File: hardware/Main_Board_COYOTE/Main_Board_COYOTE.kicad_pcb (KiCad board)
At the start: 2 copper layers, 198 x 138 mm, 57 parts, among them J1 Conn_01x05_Pin, J1 FTDI, J2 Conn_01x05_Pin, J3 Conn_01x05_Pin, J4 V+-, Q1 2N7002, SW1 SW_SPST, SW2 START, SW3 START, U1 QRE1113GR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

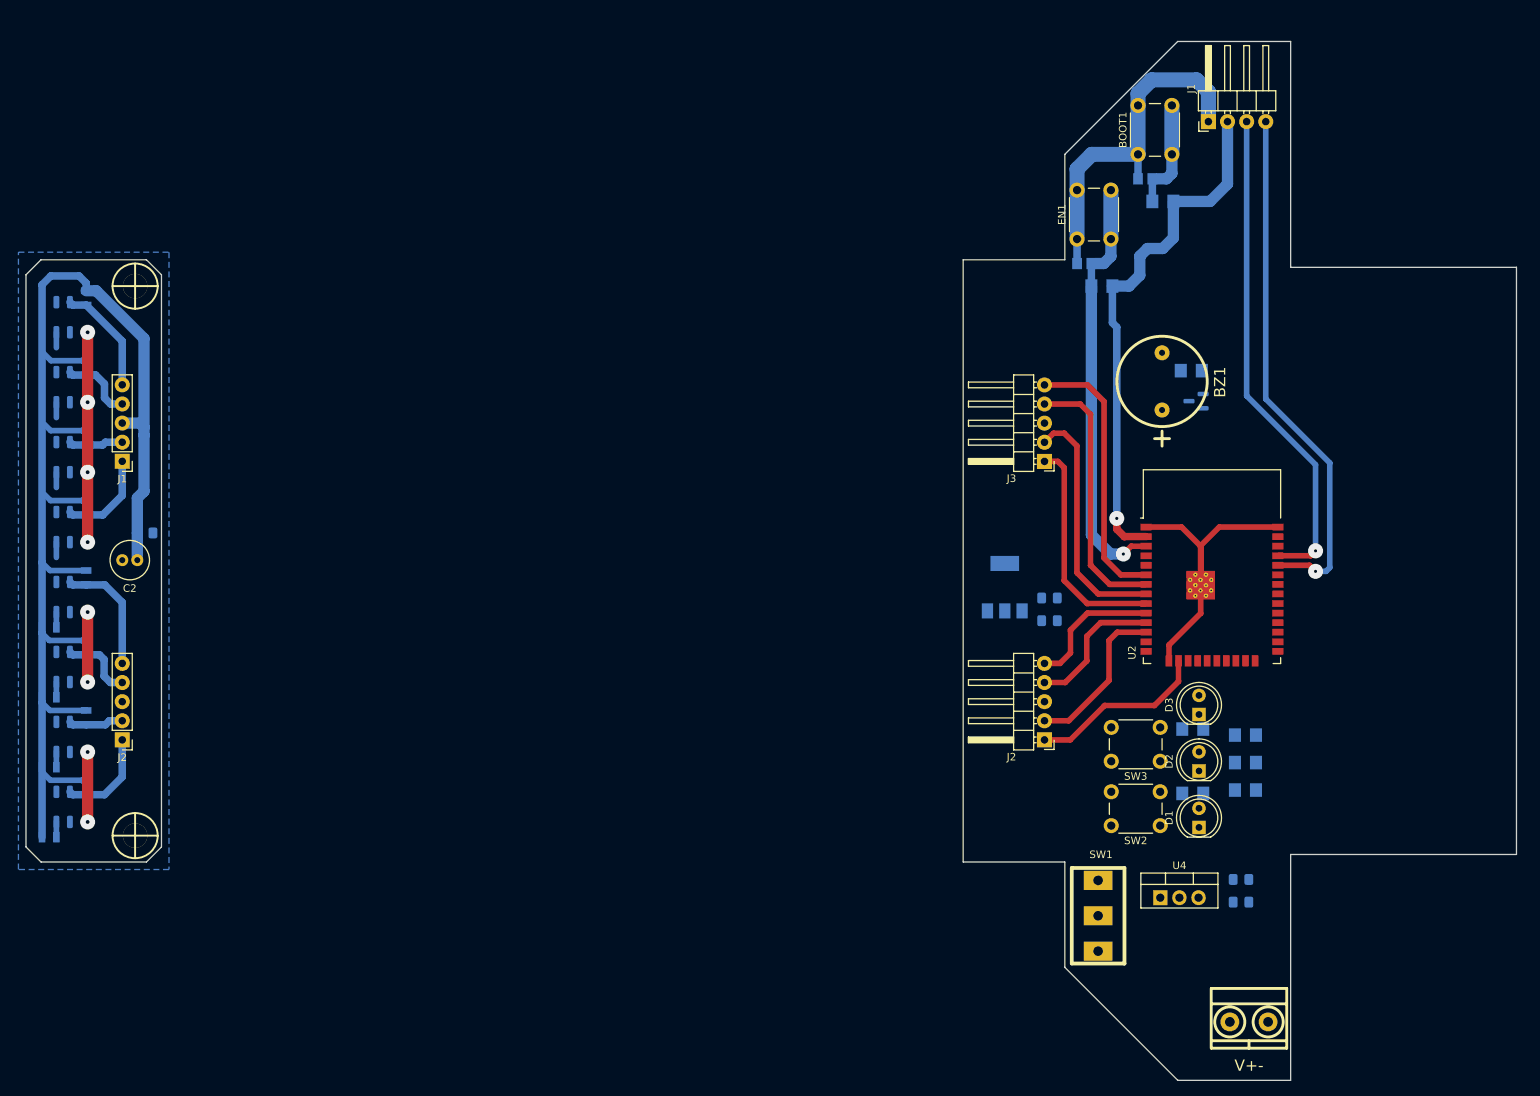
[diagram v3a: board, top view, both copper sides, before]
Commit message: SCH del velocista terminado
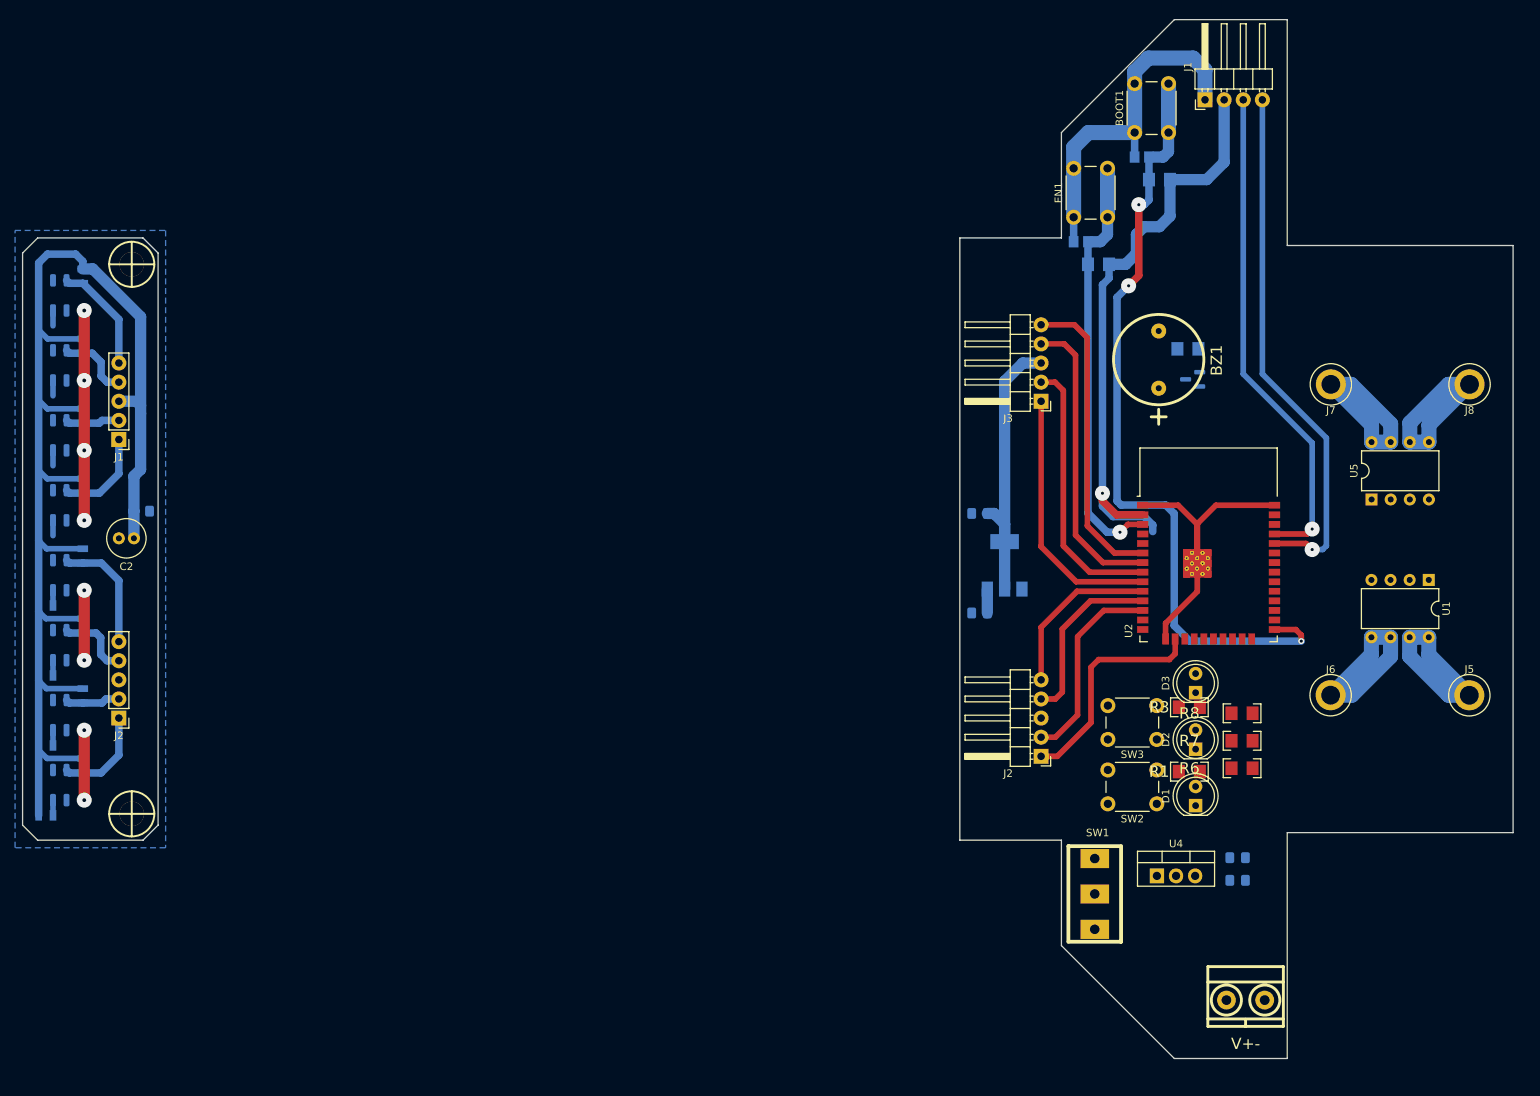
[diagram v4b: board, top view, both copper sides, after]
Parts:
- added J5: MOTOR_PINM1A, Connector:Banana_Jack_1Pin, F.Cu at (243.6, 110.8)
- added J6: MOTOR_PINM1B, Connector:Banana_Jack_1Pin, F.Cu at (225.2, 110.8)
- added J7: MOTOR_PINM1A, Connector:Banana_Jack_1Pin, F.Cu at (225.2, 69.5)
- added J8: MOTOR_PINM1B, Connector:Banana_Jack_1Pin, F.Cu at (243.6, 69.5)
- added U1: TA6586, Package_DIP:DIP-8_W7.62mm, F.Cu at (238.2, 95.5)
- added U5: TA6586, Package_DIP:DIP-8_W7.62mm, F.Cu at (230.6, 84.8)
- R1, R3, R6, R7, R8: moved to F.Cu
- moved C2 17.0 mm to (178.5, 86.7)
- moved C1 9.51 mm to (178.5, 99.9)
- moved J3 8.00 mm to (186.7, 71.8)
- moved R6 2.93 mm to (213.4, 120.5)
- moved U2 2.93 mm to (209.0, 93.8)
- moved C1 2.93 mm to (67.3, 86.4)
- moved H1 2.93 mm to (65.9, 126.6)
- moved R13 2.93 mm to (59.4, 92.3)
- moved R11 2.93 mm to (54.5, 117.5)
- moved U4 2.93 mm to (56.4, 85.6)
- moved U6 2.93 mm to (56.4, 104.2)
- moved U8 2.93 mm to (56.4, 122.7)
- moved BZ1 2.93 mm to (202.3, 66.2)
- moved C5 2.93 mm to (212.8, 132.4)
- moved D1 2.93 mm to (207.2, 125.5)
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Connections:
- R6 pad 1: /LED -> /LED_1
- R7 pad 1: /LED -> /LED_2
- R8 pad 1: /LED -> /LED_BUILTING
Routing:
- net /BOOT: track 14.3 -> 104.7 mm, vias 0 -> 3
- net +3V3: track 241.2 -> 291.2 mm
- net /OUTM1B: track 0.00 -> 25.1 mm
- net /OUTM1A: track 0.00 -> 25.1 mm
- net /OUTM2B: track 0.00 -> 25.0 mm
- net /OUTM2A: track 0.00 -> 25.0 mm
- net /OUT_8: track 23.8 -> 29.7 mm
- net /OUT_6: track 18.7 -> 23.8 mm
- net /OUT_7: track 21.5 -> 26.6 mm
- net /OUT_4: track 30.1 -> 34.7 mm
- net /OUT_1: track 36.1 -> 40.7 mm
- net /OUT_5: track 18.0 -> 22.5 mm
- net /OUT_2: track 35.2 -> 39.5 mm
- net /OUT_3: track 32.7 -> 36.1 mm
- net Net-(SW1-B): track 0.00 -> 3.18 mm
